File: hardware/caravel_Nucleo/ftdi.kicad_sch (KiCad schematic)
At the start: 26 parts

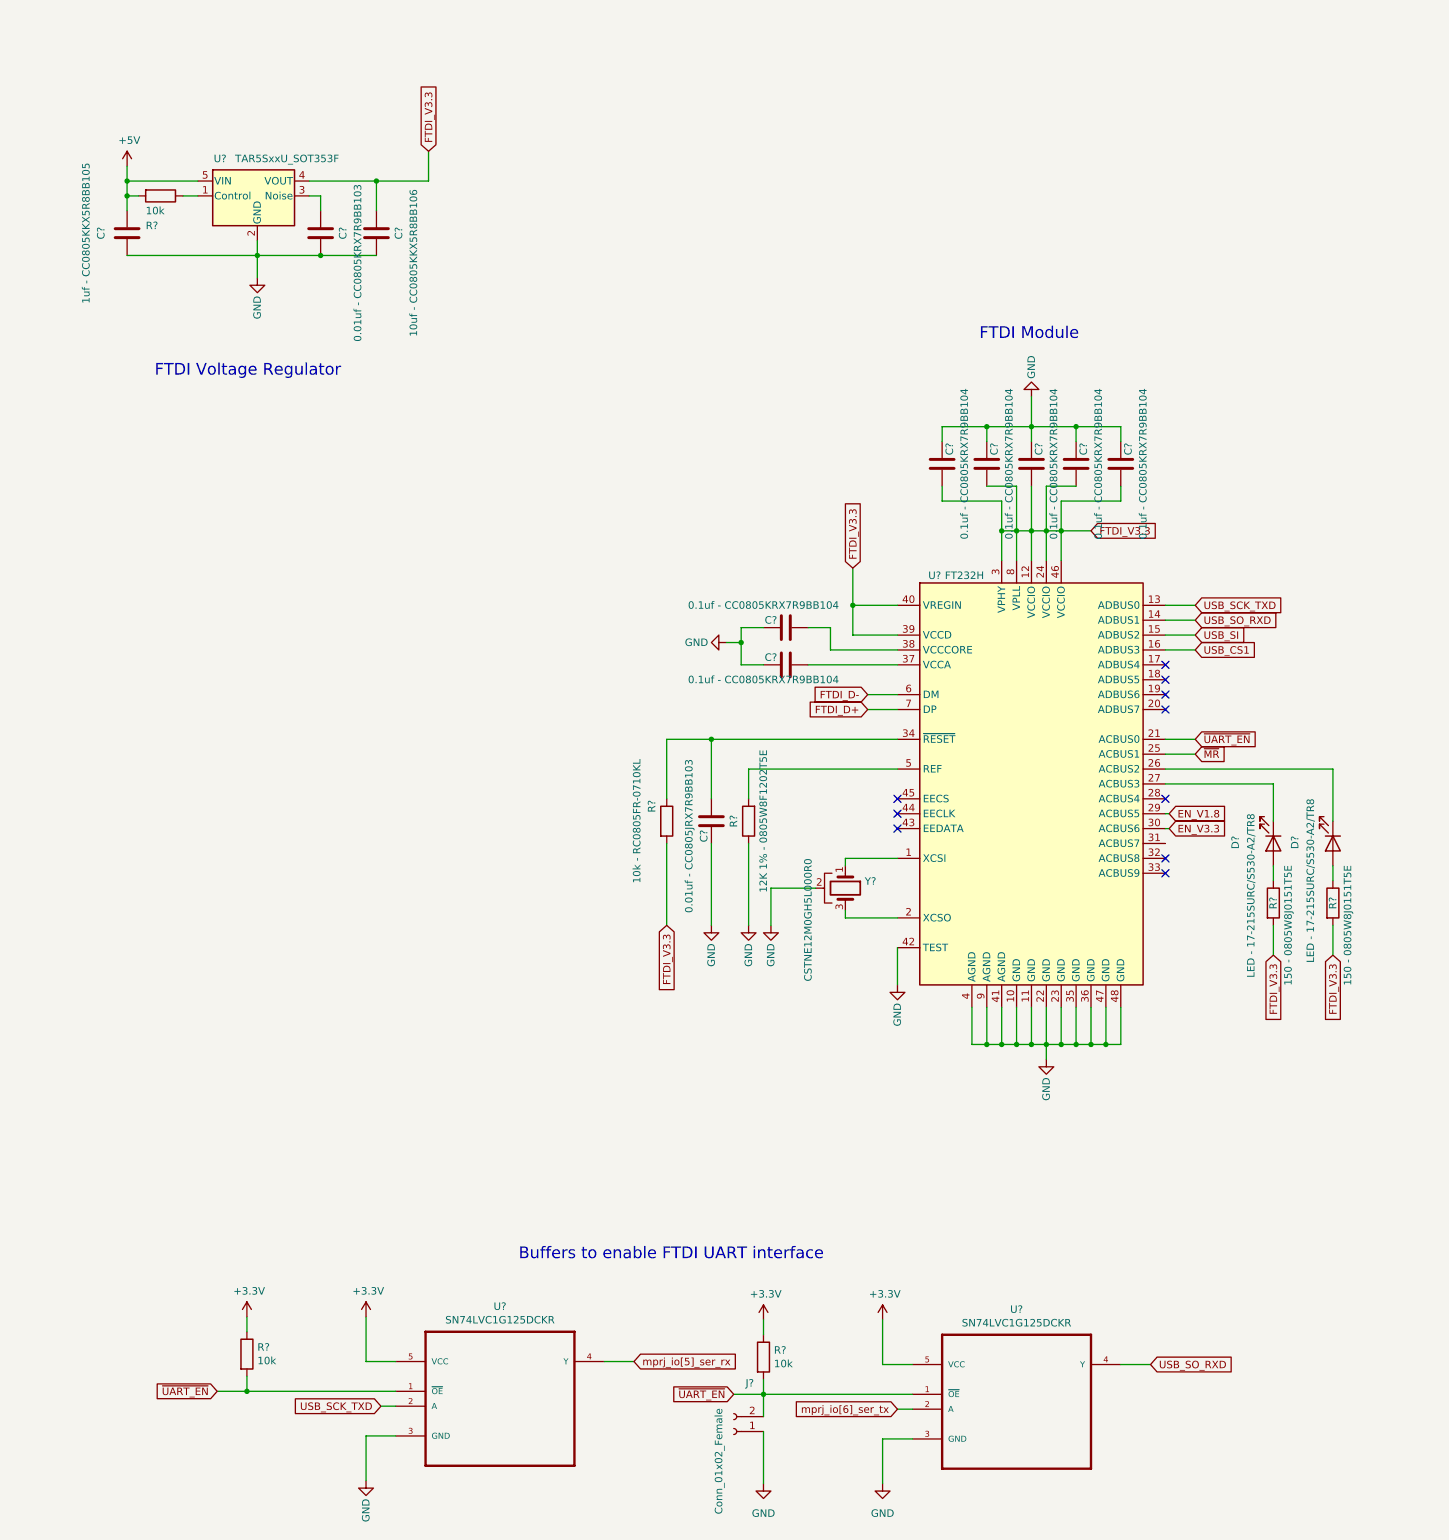
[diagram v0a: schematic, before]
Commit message: Replace components to Antmicro library ones
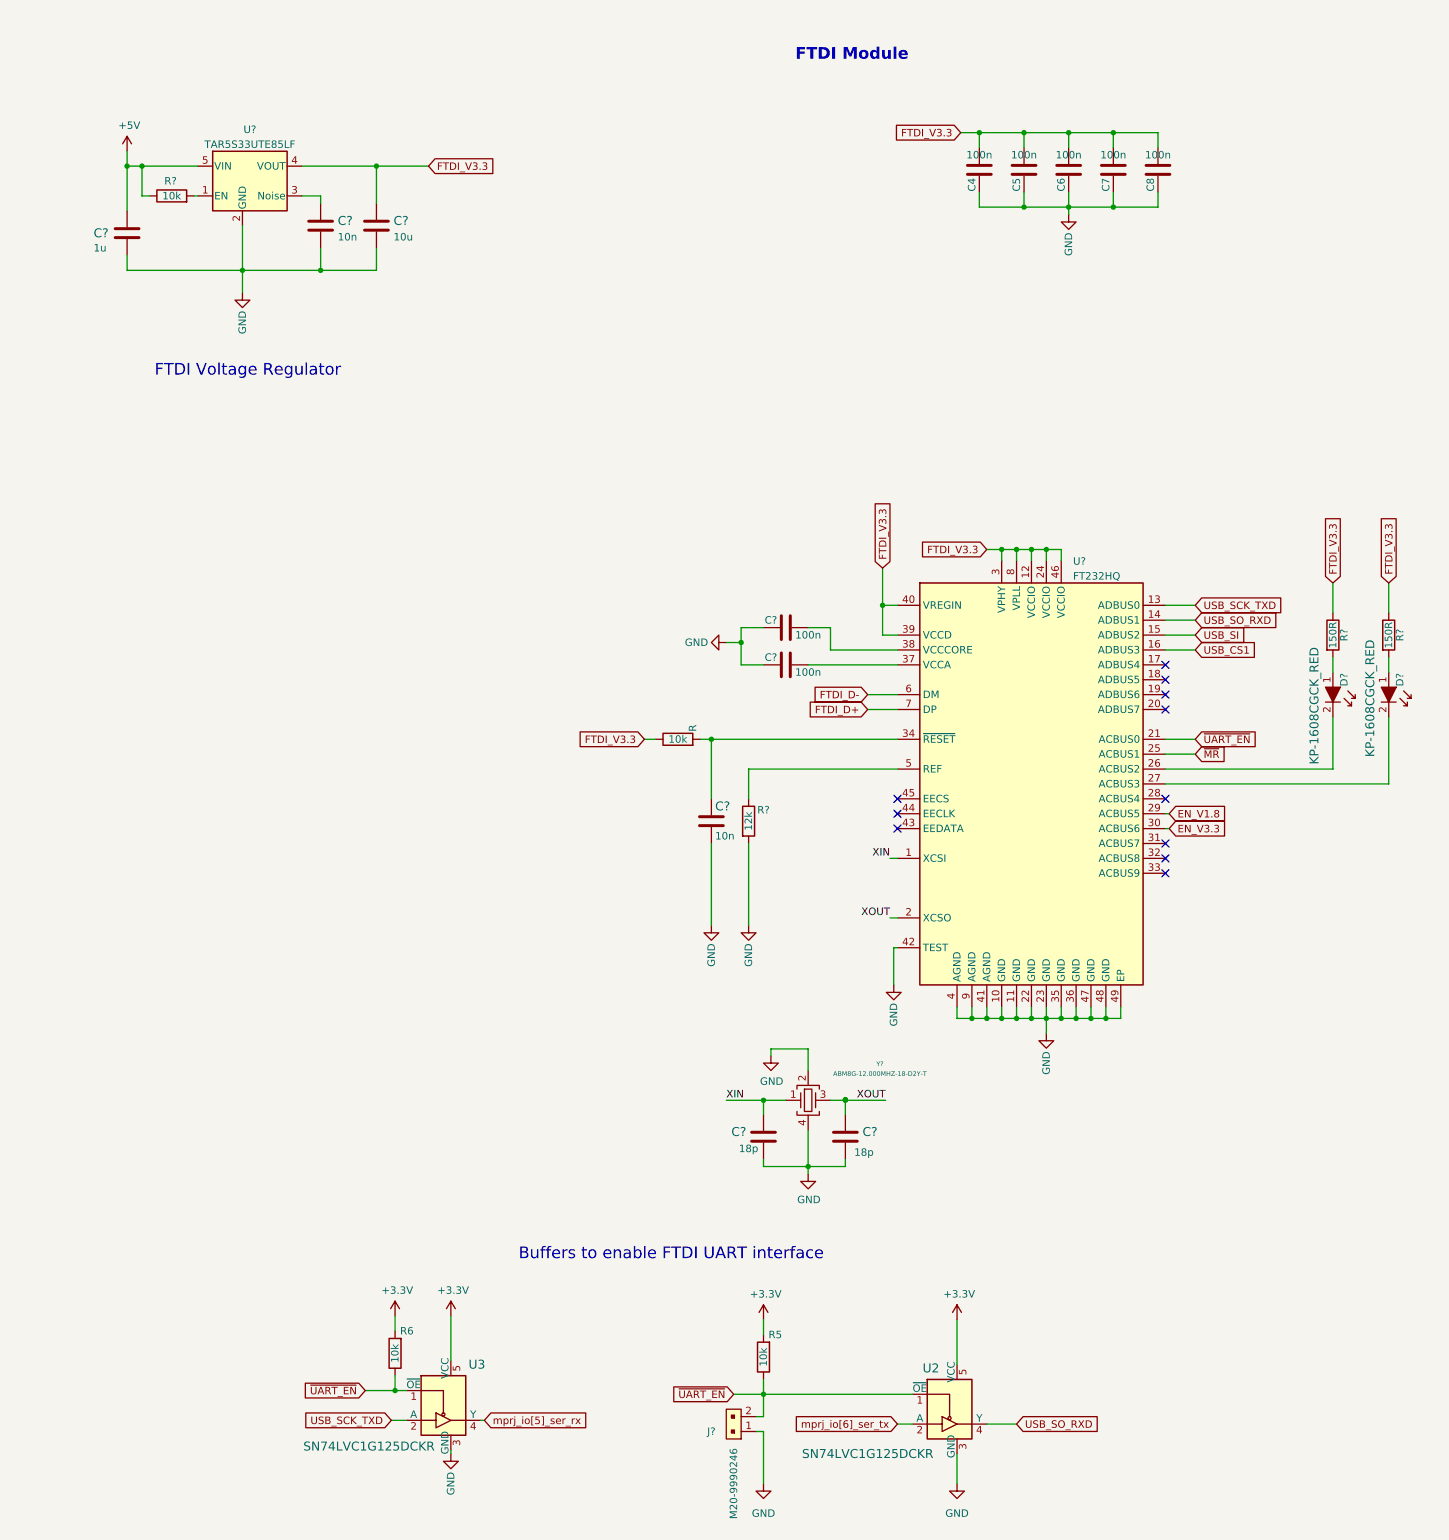
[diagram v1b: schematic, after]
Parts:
- removed C?: 0.01uf - CC0805JRX7R9BB103, Capacitor_SMD:C_0805_2012Metric, symbol Device:C
- removed C?: 1uf - CC0805KKX5R8BB105, Capacitor_SMD:C_0805_2012Metric, symbol Device:C
- removed C?: 10uf - CC0805KKX5R8BB106, Capacitor_SMD:C_0805_2012Metric, symbol Device:C
- removed C?: 0.01uf - CC0805KRX7R9BB103, Capacitor_SMD:C_0805_2012Metric, symbol Device:C
- removed J?: Conn_01x02_Female, Connector_PinHeader_2.54mm:PinHeader_1x02_P2.54mm_Vertical, symbol Connector:Conn_01x02_Female
- removed U?: FT232H, Package_DFN_QFN:QFN-48-1EP_8x8mm_P0.5mm_EP6.2x6.2mm, symbol Interface_USB:FT232H
- removed U? (x2): SN74LVC1G125DCKR, SOT65P210X110-5N, symbol Caravel_board:SN74LVC1G125DCKR
- removed U?: TAR5SxxU_SOT353F, Caravel_Board:SOT-353F, symbol Caravel_board:TAR5SxxU_SOT353F
- removed Y?: CSTNE12M0GH5L000R0, strive_foot_prints:CSTNE12M0GH5L000R0, symbol Device:Crystal_GND2
- added C?: C_1u_0805, antmicro-footprints:0805-cap, symbol antmicroCapacitorsmisc:C_1u_0805
- added C? (x2): C_18p_0603, antmicro-footprints:0603-cap, symbol antmicroCapacitors0603:C_18p_0603
- added C?: C_10u_0805, antmicro-footprints:0805-cap, symbol antmicroCapacitorsmisc:C_10u_0805
- added C? (x2): C_10n_0805, antmicro-footprints:0805-cap, symbol antmicroCapacitorsmisc:C_10n_0805
- added J?: M20-9990246, antmicro-footprints:PinHeader_1x2_P2.54mm, symbol antmicroRectangularConnectorsHeadersMalePins:M20-9990246
- added U2, U3: SN74LVC1G125DCKR, antmicro-footprints:SOT-353, symbol antmicroLogicBuffersDriversReceiversTransceivers:SN74LVC1G125DCKR
- added U?: TAR5S33UTE85LF, antmicro-footprints:SOT-353, symbol antmicroPMICVoltageRegulatorsLinear:TAR5S33UTE85LF
- added U?: FT232HQ, antmicro-footprints:QFN-48-1EP_6x6mm, symbol antmicroInterfaceControllers:FT232HQ
- added Y?: ABM8G-12.000MHZ-18-D2Y-T, antmicro-footprints:KX-7, symbol antmicroCrystals:ABM8G-12.000MHZ-18-D2Y-T
- C4, C5, C6, C7, C8: renamed from C?; value 0.1uf - CC0805KRX7R9BB104 -> C_100n_0603; footprint Capacitor_SMD:C_0805_2012Metric -> antmicro-footprints:0603-cap; symbol Device:C -> antmicroCapacitors0603:C_100n_0603; MPN (none) -> 0603YC104KAZ2A; Manufacturer (none) -> AVX; Val (none) -> 100n
- C? (x2): value 0.1uf - CC0805KRX7R9BB104 -> C_100n_0603; footprint Capacitor_SMD:C_0805_2012Metric -> antmicro-footprints:0603-cap; symbol Device:C -> antmicroCapacitors0603:C_100n_0603; MPN (none) -> 0603YC104KAZ2A; Manufacturer (none) -> AVX; Val (none) -> 100n
- D? (x2): value LED - 17-215SURC/S530-A2/TR8 -> KP-1608CGCK_RED; footprint LED_SMD:LED_1206_3216Metric -> antmicro-footprints:LED0603_RED; symbol Device:LED -> antmicroLEDIndicationDiscrete:KP-1608CGCK_RED; MPN (none) -> KP-1608CGCK; Manufacturer (none) -> KINGBRIGHT
- R: renamed from R?; value 10k - RC0805FR-0710KL -> R_10k_0603; footprint Resistor_SMD:R_0805_2012Metric -> antmicro-footprints:0603-res; symbol Device:R -> antmicroResistors0603:R_10k_0603; MPN (none) -> CR0603-JW-103ELF; Manufacturer (none) -> BOURNS; Val (none) -> 10k
- R5, R6: renamed from R?; value 10k -> R_10k_0603; footprint Resistor_SMD:R_0805_2012Metric -> antmicro-footprints:0603-res; symbol Device:R -> antmicroResistors0603:R_10k_0603; MPN (none) -> CR0603-JW-103ELF; Manufacturer (none) -> BOURNS; Val (none) -> 10k
- R? (x2): value 150 - 0805W8J0151T5E -> R_150R_0603; footprint Resistor_SMD:R_0805_2012Metric -> antmicro-footprints:0603-res; symbol Device:R -> antmicroResistors0603:R_150R_0603; MPN (none) -> MC0063W06031150R; Manufacturer (none) -> MULTICOMP; Val (none) -> 150R
- R?: value 12K 1% - 0805W8F1202T5E -> R_12k_0603; footprint Resistor_SMD:R_0805_2012Metric -> antmicro-footprints:0603-res; symbol Device:R -> antmicroResistors0603:R_12k_0603; MPN (none) -> CR0603-FX-1202ELF; Manufacturer (none) -> BOURNS; Val (none) -> 12k
- R?: value 10k -> R_10k_0603; footprint Resistor_SMD:R_0805_2012Metric -> antmicro-footprints:0603-res; symbol Device:R -> antmicroResistors0603:R_10k_0603; MPN (none) -> CR0603-JW-103ELF; Manufacturer (none) -> BOURNS; Val (none) -> 10k
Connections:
- net +3V3: now also R5.2, R6.2, U2.5 (VCC), U3.5 (VCC); no longer R5.1, R6.1
- net +5V: now also R?.1, C?.1, U?.5 (VIN); no longer R?.2
- net EN_V1.8: now also U?.29 (ACBUS5)
- net EN_V3.3: now also U?.30 (ACBUS6)
- net FTDI_D+: now also U?.7 (DP)
- net FTDI_D-: now also U?.6 (DM)
- net FTDI_V3.3: now also R.1, R?.1, R?.1, C?.1, U?.12 (VCCIO), U?.24 (VCCIO), U?.3 (VPHY), U?.39 (VCCD), U?.4 (VOUT), U?.40 (VREGIN), U?.46 (VCCIO), U?.8 (VPLL); no longer R.2, R?.2, R?.2
- net GND: now also R?.2, C?.2, C?.2, C?.2, C?.2, C?.2, C?.2, J?.1, U2.3 (GND), U3.3 (GND), U?.10 (GND), U?.11 (GND), U?.2 (GND), U?.22 (GND), U?.23 (GND), U?.35 (GND), U?.36 (GND), U?.4 (AGND), U?.41 (AGND), U?.42 (TEST), U?.47 (GND), U?.48 (GND), U?.49 (EP), U?.9 (AGND), Y?.2, Y?.4; no longer R?.1
- net USB_CS1: now also U?.16 (ADBUS3)
- net USB_SCK_TXD: now also U3.2 (A), U?.13 (ADBUS0)
- net USB_SI: now also U?.15 (ADBUS2)
- net USB_SO_RXD: now also U2.4 (Y), U?.14 (ADBUS1)
- net mprj_io[5]_ser_rx: now also U3.4 (Y)
- net mprj_io[6]_ser_tx: now also U2.2 (A)
- net ~{MR}: now also U?.25 (ACBUS1)
- net ~{UART_EN}: now also R5.1, R6.1, J?.2, U2.1 (~{OE}), U3.1 (~{OE}), U?.21 (ACBUS0); no longer R5.2, R6.2
- net at D?.1: now also R?.2 (x2)
- net at C?.2: now also U?.37 (VCCA)
- net at C?.2: now also U?.38 (VCCCORE)
- net at D?.2: now also U?.27 (ACBUS3); no longer R?.1
- net at D?.2: now also U?.26 (ACBUS2); no longer R?.1
- new net: R?.2, U?.1 (EN)
- new net: C?.1, U?.3 (Noise)
- new net: C?.1, R.2, U?.34 (~{RESET})
- new net: R?.1, U?.5 (REF)
- new net XIN: C?.1, U?.1 (XCSI), Y?.1
- new net XOUT: C?.1, U?.2 (XCSO), Y?.3
- no-connect marks 10 -> 11
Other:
- moved on the sheet: C4, C5, C6, C7, C8, R, R5, R6, R?

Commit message: Finished changing symbols to antmicro global library
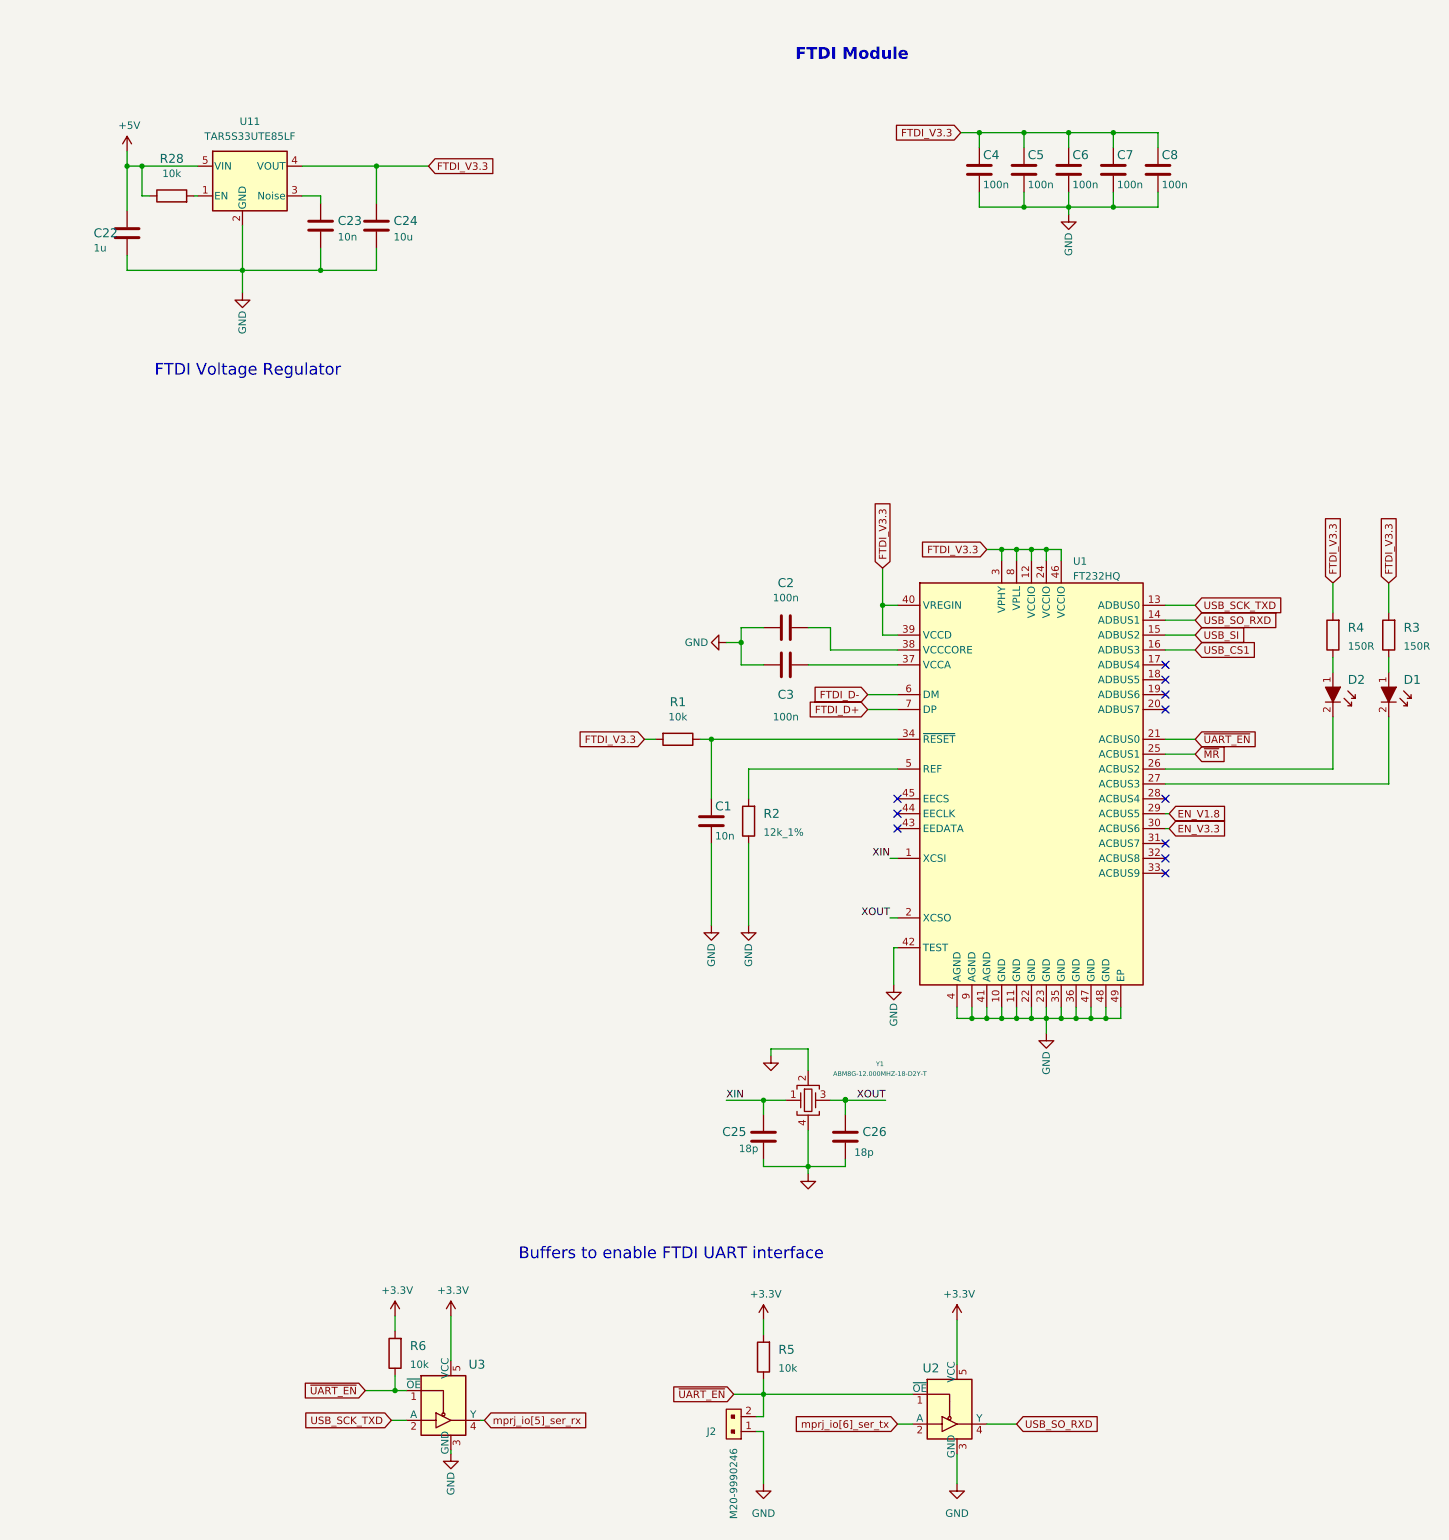
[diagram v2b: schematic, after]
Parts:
- removed C? (x2): C_100n_0603, antmicro-footprints:0603-cap, symbol antmicroCapacitors0603:C_100n_0603
- removed D? (x2): KP-1608CGCK_RED, antmicro-footprints:LED0603_RED, symbol antmicroLEDIndicationDiscrete:KP-1608CGCK_RED
- removed R, R?: R_10k_0603, antmicro-footprints:0603-res, symbol antmicroResistors0603:R_10k_0603
- removed R? (x2): R_150R_0603, antmicro-footprints:0603-res, symbol antmicroResistors0603:R_150R_0603
- removed R?: R_12k_0603, antmicro-footprints:0603-res, symbol antmicroResistors0603:R_12k_0603
- removed U?: TAR5S33UTE85LF, antmicro-footprints:SOT-353, symbol antmicroPMICVoltageRegulatorsLinear:TAR5S33UTE85LF
- added C2, C3: C_100n_0603, antmicro-footprints:0603-cap, symbol antmicroCapacitors0603:C_100n_0603
- added D1, D2: KP-1608CGCK_GREEN, antmicro-footprints:LED0603_GREEN, symbol antmicroLEDIndicationDiscrete:KP-1608CGCK_GREEN
- added R1, R28: R_10k_0603, antmicro-footprints:0603-res, symbol antmicroResistors0603:R_10k_0603
- added R2: R_12k_1%_0603, antmicro-footprints:0603-res, symbol antmicroResistors0603:R_12k_1%_0603
- added R3, R4: R_150R_0603, antmicro-footprints:0603-res, symbol antmicroResistors0603:R_150R_0603
- added U11: TAR5S33UTE85LF, antmicro-footprints:SOT-353, symbol antmicroPMICVoltageRegulatorsLinear:TAR5S33UTE85LF
- C25, C26: renamed from C?; value C_18p_0603 -> (none); footprint antmicro-footprints:0603-cap -> (none)
- U2, U3: value SN74LVC1G125DCKR -> (none); footprint antmicro-footprints:SOT-353 -> (none)
- gave numbers to parts that had none: 7
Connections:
- net +5V: now also R28.1, U11.5 (VIN)
- net FTDI_V3.3: now also C4.1, C5.1, C6.1, C7.1, C8.1, R1.2, R3.2, R4.2, U11.4 (VOUT); no longer C4.2, C5.2, C6.2, C7.2, C8.2
- net GND: now also C4.2, C5.2, C6.2, C7.2, C8.2, C2.1, C3.1, R2.1, U11.2 (GND); no longer C4.1, C5.1, C6.1, C7.1, C8.1
- net at C23.1: now also U11.3 (Noise)
- net at U1.27 (ACBUS3): now also D1.2
- net at C1.1, U1.34 (~{RESET}): now also R1.1
- net at U1.5 (REF): now also R2.2
- net at U1.37 (VCCA): now also C3.2
- net at U1.38 (VCCCORE): now also C2.2
- net at U1.26 (ACBUS2): now also D2.2
- new net: R28.2, U11.1 (EN)
- new net: D2.1, R4.1
- new net: D1.1, R3.1
